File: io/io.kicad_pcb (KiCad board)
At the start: 4 copper layers, 84 x 40 mm, 48 parts, among them J2 Conn_02x03, J3 QwST, J4 SM03B-SRSS-TB, J5 QwST, J6 Conn_02x08_Odd_Even, SW1 SW_Push, SW2 SW_Push, U1 RP2350_80QFN, U2 74LVC32, U3 W25Q32JVS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

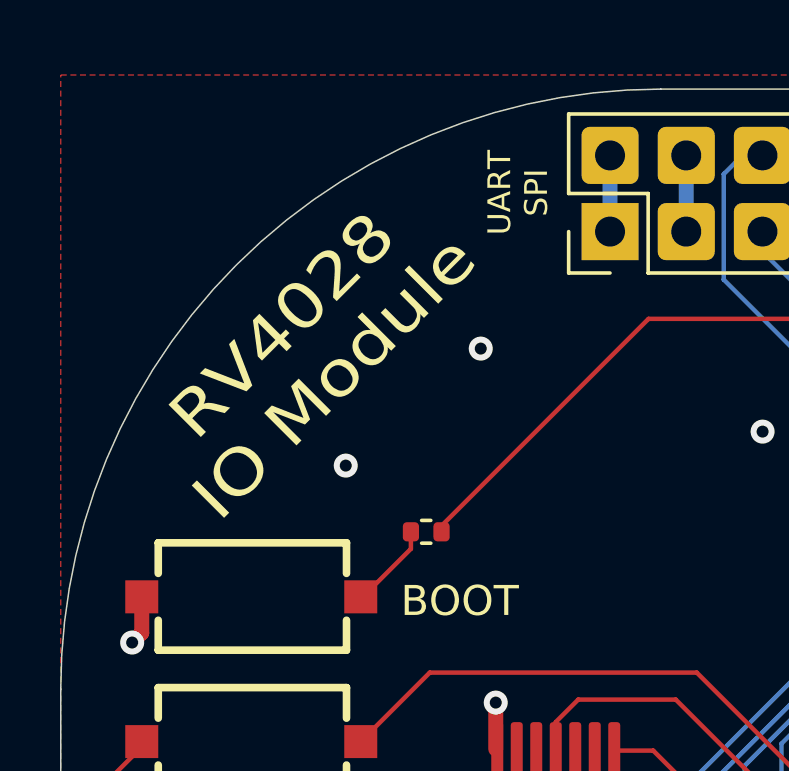
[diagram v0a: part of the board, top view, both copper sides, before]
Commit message: Finish RAM module routing
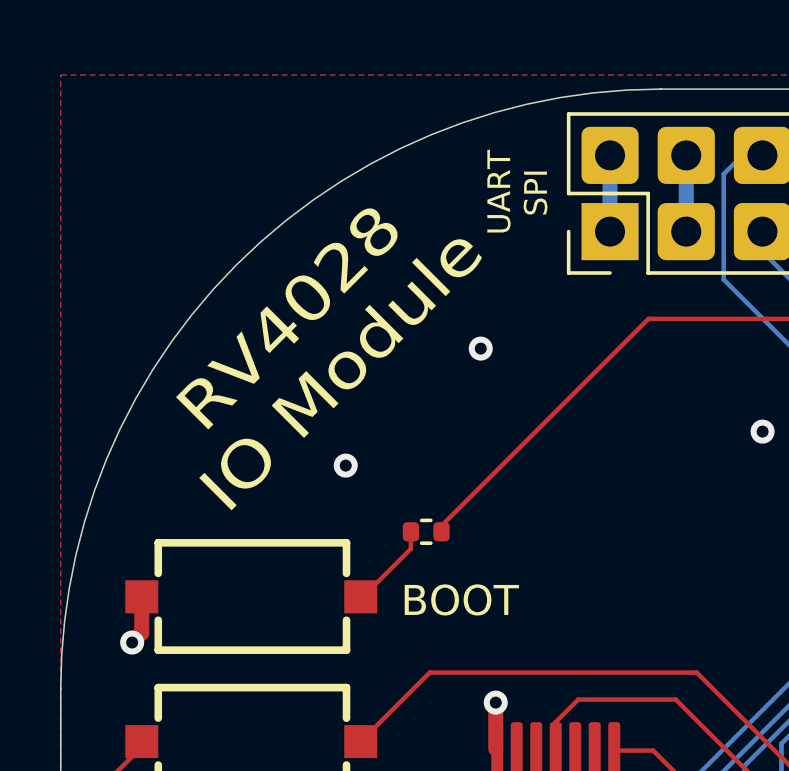
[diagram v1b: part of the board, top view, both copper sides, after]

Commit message: Review before first PCB order
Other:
- board text removed: "~{BRQ}"
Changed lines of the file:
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@@
+			)
+		)
+		(property "JLC" "C5383108"
+			(at 0 0 90)
+			(unlocked yes)
+			(layer "F.Fab")
+			(hide yes)
+			(effects
+				(font
+					(size 1 1)
+					(thickness 0.15)
+				)
 			)
 		)
@@
 				(font
 					(size 1.27 1.27)
+					(thickness 0.15)
+				)
+			)
+		)
+		(property "JLC" "C5383104"
+			(at 0 0 0)
+			(unlocked yes)
+			(layer "F.Fab")
+			(hide yes)
+			(effects
+				(font
+					(size 1 1)
 					(thickness 0.15)
 				)
@@
 	)
 	(gr_text "RV2048 IO v0.1\n© Michael Bell 2026\nJLCJLCJLCJLC"
-		(at 175 101.75 90)
+		(at 170 101.75 90)
 		(layer "B.SilkS")
 		(effects
@@
 		)
 	)
-	(gr_text "~{BRQ}"
-		(at 141.4 114.9 90)
-		(layer "B.SilkS")
-		(effects
-			(font
-				(size 0.635 0.635)
-				(thickness 0.1016)
-			)
-			(justify right bottom mirror)
-		)
-	)
